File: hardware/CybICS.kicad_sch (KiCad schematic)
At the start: 64 parts, among them J1 Raspberry_Pi_2_3, J2 Conn_01x03_Pin, J3 Conn_01x05_Pin, SW1 SW_Push, SW2 SW_Push, U1 STM32G070RBTx

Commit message: Updated hardware
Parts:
- added R28: 10kR, Resistor_SMD:R_0805_2012Metric_Pad1.20x1.40mm_HandSolder, symbol Device:R
- J1: footprint Connector_PinHeader_2.54mm:PinHeader_2x20_P2.54mm_Vertical -> Module:Raspberry_Pi_Zero_Socketed_THT_FaceDown_MountingHoles
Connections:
- net GND: now also R28.2
- net PC10: now also R28.1
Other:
- moved on the sheet: R27, SW2
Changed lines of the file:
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@@
   (junction (at 64.77 24.13) (diameter 0) (color 0 0 0 0)
   )
+  (junction (at 156.21 181.61) (diameter 0) (color 0 0 0 0)
+  )
   (junction (at 161.29 100.33) (diameter 0) (color 0 0 0 0)
   )
@@
     (stroke (width 0) (type default))
   )
-  (wire (pts (xy 134.62 181.61) (xy 134.62 179.07))
+  (wire (pts (xy 165.1 171.45) (xy 165.1 170.18))
     (stroke (width 0) (type default))
   )
@@
     (stroke (width 0) (type default))
   )
-  (wire (pts (xy 123.19 191.77) (xy 134.62 191.77))
+  (wire (pts (xy 153.67 181.61) (xy 156.21 181.61))
     (stroke (width 0) (type default))
   )
@@
     (stroke (width 0) (type default))
   )
-  (polyline (pts (xy 113.03 140.97) (xy 113.03 196.85))
+  (polyline (pts (xy 113.03 140.97) (xy 113.03 170.18))
     (stroke (width 0) (type default))
   )
@@
     (stroke (width 0) (type default))
   )
+  (wire (pts (xy 156.21 181.61) (xy 165.1 181.61))
+    (stroke (width 0) (type default))
+  )
   (wire (pts (xy 271.78 149.86) (xy 281.94 149.86))
     (stroke (width 0) (type default))
@@
     (stroke (width 0) (type default))
   )
+  (polyline (pts (xy 146.05 160.02) (xy 180.34 160.02))
+    (stroke (width 0) (type default))
+  )
   (wire (pts (xy 271.78 152.4) (xy 281.94 152.4))
     (stroke (width 0) (type default))
@@
     (stroke (width 0) (type default))
   )
-  (wire (pts (xy 132.08 181.61) (xy 134.62 181.61))
+  (wire (pts (xy 162.56 171.45) (xy 165.1 171.45))
     (stroke (width 0) (type default))
   )
@@
     (stroke (width 0) (type default))
   )
-  (wire (pts (xy 124.46 181.61) (xy 123.19 181.61))
+  (wire (pts (xy 154.94 171.45) (xy 153.67 171.45))
     (stroke (width 0) (type default))
   )
@@
     (effects (font (size 1.27 1.27)) (justify left bottom))
   )
-  (text "Button" (at 114.3 172.72 0)
+  (text "Button" (at 147.32 163.83 0)
     (effects (font (size 1.27 1.27)) (justify left bottom))
   )
@@
     (effects (font (size 1.27 1.27)) (justify left bottom))
   )
-  (label "PC10" (at 129.54 191.77 0) (fields_autoplaced)
+  (label "PC10" (at 160.02 181.61 0) (fields_autoplaced)
     (effects (font (size 1.27 1.27)) (justify left bottom))
   )
@@
     )
   )
+  (symbol (lib_id "Device:R") (at 156.21 185.42 0) (unit 1)
+    (in_bom yes) (on_board yes) (dnp no)
+    (property "Reference" "R28" (at 158.75 184.15 0)
+      (effects (font (size 1.27 1.27)) (justify left))
+    )
+    (property "Value" "10kR" (at 158.75 186.69 0)
+      (effects (font (size 1.27 1.27)) (justify left))
+    )
+    (property "Footprint" "Resistor_SMD:R_0805_2012Metric_Pad1.20x1.40mm_HandSolder" (at 154.432 185.42 90)
+      (effects (font (size 1.27 1.27)) hide)
+    )
+    (property "Datasheet" "~" (at 156.21 185.42 0)
+      (effects (font (size 1.27 1.27)) hide)
+    )
+    (property "JLCPCB Part #" "C17513" (at 156.21 185.42 90)
+      (effects (font (size 1.27 1.27)) hide)
+    )
+    (pin "2")
+    (pin "1")
+    (instances
+      (project "CybICS"
+        (path "/8fcde287-628f-41a4-bd3a-47641b4dabbc"
+          (reference "R28") (unit 1)
+        )
+      )
+    )
+  )
   (symbol (lib_id "Device:R") (at 88.9 153.67 90) (unit 1)
     (in_bom yes) (on_board yes) (dnp no) (fields_autoplaced)
@@
     )
   )
-  (symbol (lib_id "Switch:SW_Push") (at 123.19 186.69 90) (unit 1)
+  (symbol (lib_id "Switch:SW_Push") (at 153.67 176.53 90) (unit 1)
     (in_bom yes) (on_board yes) (dnp no) (fields_autoplaced)
-    (property "Reference" "SW2" (at 124.46 185.42 90)
+    (property "Reference" "SW2" (at 154.94 175.26 90)
       (effects (font (size 1.27 1.27)) (justify right))
     )
-    (property "Value" "SW_Push" (at 124.46 187.96 90)
+    (property "Value" "SW_Push" (at 154.94 177.8 90)
       (effects (font (size 1.27 1.27)) (justify right))
     )
-    (property "Footprint" "Button_Switch_THT:SW_PUSH_6mm_H5mm" (at 118.11 186.69 0)
+    (property "Footprint" "Button_Switch_THT:SW_PUSH_6mm_H5mm" (at 148.59 176.53 0)
       (effects (font (size 1.27 1.27)) hide)
     )
-    (property "Datasheet" "~" (at 118.11 186.69 0)
+    (property "Datasheet" "~" (at 148.59 176.53 0)
       (effects (font (size 1.27 1.27)) hide)
     )
-    (property "JLCPCB Part #" "C428628" (at 123.19 186.69 90)
+    (property "JLCPCB Part #" "C428628" (at 153.67 176.53 90)
       (effects (font (size 1.27 1.27)) hide)
     )
@@
     )
   )
+  (symbol (lib_id "power:GND") (at 156.21 189.23 0) (unit 1)
+    (in_bom yes) (on_board yes) (dnp no) (fields_autoplaced)
+    (property "Reference" "#PWR041" (at 156.21 195.58 0)
+      (effects (font (size 1.27 1.27)) hide)
+    )
+    (property "Value" "GND" (at 156.21 194.31 0)
+      (effects (font (size 1.27 1.27)))
+    )
+    (property "Footprint" "" (at 156.21 189.23 0)
+      (effects (font (size 1.27 1.27)) hide)
+    )
+    (property "Datasheet" "" (at 156.21 189.23 0)
+      (effects (font (size 1.27 1.27)) hide)
+    )
+    (pin "1")
+    (instances
+      (project "CybICS"
+        (path "/8fcde287-628f-41a4-bd3a-47641b4dabbc"
+          (reference "#PWR041") (unit 1)
+        )
+      )
+    )
+  )
   (symbol (lib_id "power:+3V3") (at 73.66 162.56 0) (unit 1)
     (in_bom yes) (on_board yes) (dnp no) (fields_autoplaced)
@@
       (effects (font (size 1.27 1.27)) (justify left))
     )
-    (property "Footprint" "Connector_PinHeader_2.54mm:PinHeader_2x20_P2.54mm_Vertical" (at 166.37 67.31 0)
+    (property "Footprint" "Module:Raspberry_Pi_Zero_Socketed_THT_FaceDown_MountingHoles" (at 166.37 67.31 0)
       (effects (font (size 1.27 1.27)) hide)
     )
@@
     )
   )
-  (symbol (lib_id "power:+3V3") (at 134.62 179.07 0) (unit 1)
+  (symbol (lib_id "power:+3V3") (at 165.1 170.18 0) (unit 1)
     (in_bom yes) (on_board yes) (dnp no) (fields_autoplaced)
-    (property "Reference" "#PWR039" (at 134.62 182.88 0)
+    (property "Reference" "#PWR039" (at 165.1 173.99 0)
       (effects (font (size 1.27 1.27)) hide)
     )
-    (property "Value" "+3V3" (at 134.62 173.99 0)
+    (property "Value" "+3V3" (at 165.1 165.1 0)
       (effects (font (size 1.27 1.27)))
     )
-    (property "Footprint" "" (at 134.62 179.07 0)
+    (property "Footprint" "" (at 165.1 170.18 0)
       (effects (font (size 1.27 1.27)) hide)
     )
-    (property "Datasheet" "" (at 134.62 179.07 0)
+    (property "Datasheet" "" (at 165.1 170.18 0)
       (effects (font (size 1.27 1.27)) hide)
     )
@@
     )
   )
-  (symbol (lib_id "Device:R") (at 128.27 181.61 270) (unit 1)
+  (symbol (lib_id "Device:R") (at 158.75 171.45 270) (unit 1)
     (in_bom yes) (on_board yes) (dnp no) (fields_autoplaced)
-    (property "Reference" "R27" (at 128.27 175.26 90)
+    (property "Reference" "R27" (at 158.75 165.1 90)
       (effects (font (size 1.27 1.27)))
     )
-    (property "Value" "1kR" (at 128.27 177.8 90)
+    (property "Value" "1kR" (at 158.75 167.64 90)
       (effects (font (size 1.27 1.27)))
     )
-    (property "Footprint" "Resistor_SMD:R_0805_2012Metric_Pad1.20x1.40mm_HandSolder" (at 128.27 179.832 90)
+    (property "Footprint" "Resistor_SMD:R_0805_2012Metric_Pad1.20x1.40mm_HandSolder" (at 158.75 169.672 90)
       (effects (font (size 1.27 1.27)) hide)
     )
-    (property "Datasheet" "~" (at 128.27 181.61 0)
+    (property "Datasheet" "~" (at 158.75 171.45 0)
       (effects (font (size 1.27 1.27)) hide)
     )
-    (property "JLCPCB Part #" "C17513" (at 128.27 181.61 90)
+    (property "JLCPCB Part #" "C17513" (at 158.75 171.45 90)
       (effects (font (size 1.27 1.27)) hide)
     )

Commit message: Updated hardware
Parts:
- added R29, R30, R31, R32, R33, R34, R35, R36: 10kR, Resistor_SMD:R_0805_2012Metric_Pad1.20x1.40mm_HandSolder, symbol Device:R
- added R37: 1kR, Resistor_SMD:R_0805_2012Metric_Pad1.20x1.40mm_HandSolder, symbol Device:R
- added SW3: SW_Push, Button_Switch_THT:SW_PUSH_6mm_H5mm, symbol Switch:SW_Push
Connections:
- net +3V3: now also R37.1
- net GND: now also R29.2, R30.2, R31.2, R32.2, R33.2, R34.2, R35.2, R36.2
- net PA0: now also R29.1
- net PA1: now also R30.1
- net PA2: now also R31.1
- net PA3: now also R32.1
- net PA4: now also R33.1
- net PA5: now also R34.1
- net PA6: now also R35.1
- net PA8: now reaches U1.36 (PA8)
- net PA8: now also R36.1, SW3.1
- new net: R37.2, SW3.2
- no-connect marks 40 -> 39
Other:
- note added: "Pulldowns"

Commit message: Add testing for i2c communication
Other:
- note added: "Button Display"
- moved on the sheet: DS1, R36, R37, RV1, SW3

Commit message: Updated documentation and preparing signals for OpenPLC
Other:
- note added: "BO_sen"
- note added: "C_sig"
- note added: "SV_sig"
- note added: "S_sen"
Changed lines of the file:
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@@
+    (effects (font (size 1.27 1.27)) (justify left bottom))
+  )
+  (text "C_sig" (at 194.31 72.39 0)
+    (effects (font (size 1.27 1.27)) (justify left bottom))
+  )
+  (text "SV_sig" (at 194.31 69.85 0)
+    (effects (font (size 1.27 1.27)) (justify left bottom))
+  )
+  (text "S_sen" (at 194.31 46.99 0)
+    (effects (font (size 1.27 1.27)) (justify left bottom))
+  )
+  (text "BO_sen" (at 194.31 85.09 0)
     (effects (font (size 1.27 1.27)) (justify left bottom))
   )

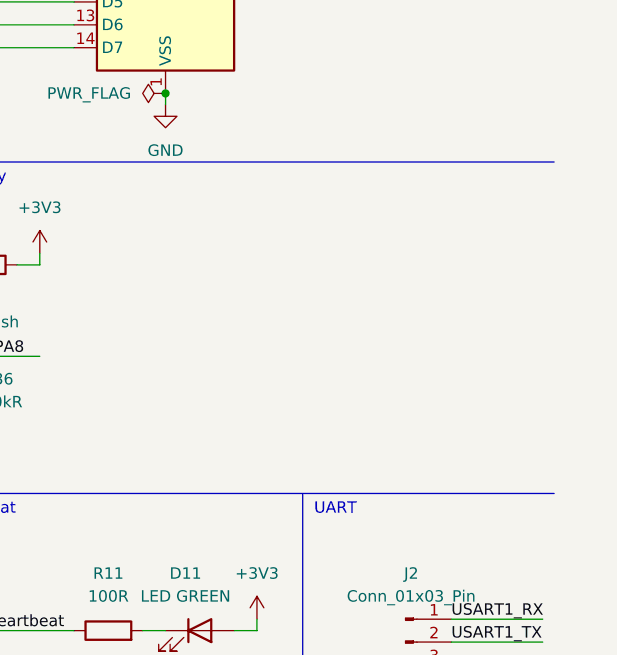
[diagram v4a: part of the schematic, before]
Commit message: This commit will: - fix #2 - Added usb-c (only for power supply) - Added first attack example
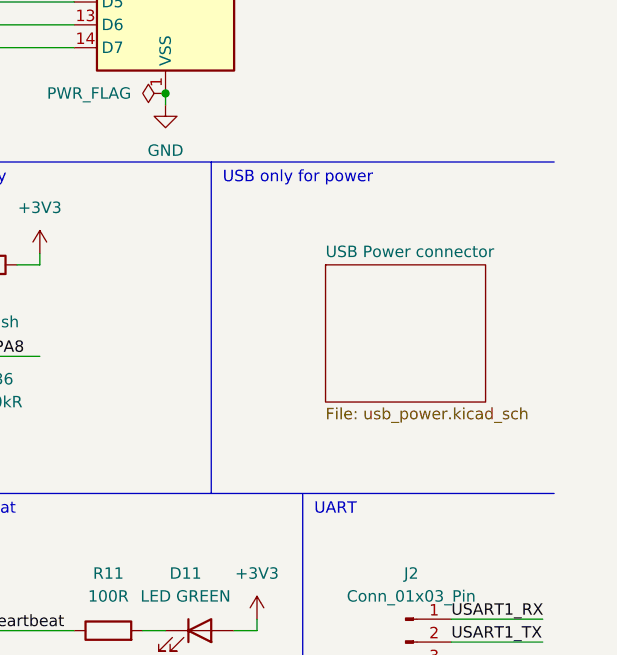
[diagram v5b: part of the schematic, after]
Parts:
- R28, R29, R30, R31, R32, R33, R34, R35, R36: JLCPCB Part # C17513 -> C17414
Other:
- added sheet USB Power connector (usb_power.kicad_sch)
- note added: "USB only for power"
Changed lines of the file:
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@@
     (stroke (width 0) (type default))
   )
+  (polyline (pts (xy 246.38 69.85) (xy 246.38 106.68))
+    (stroke (width 0) (type default))
+  )
   (polyline (pts (xy 256.54 106.68) (xy 256.54 165.1))
     (stroke (width 0) (type default))
@@
     (effects (font (size 1.27 1.27)) (justify left bottom))
   )
+  (text "USB only for power" (at 247.65 72.39 0)
+    (effects (font (size 1.27 1.27)) (justify left bottom))
+  )
   (text "Blowout" (at 13.97 143.51 0)
     (effects (font (size 1.27 1.27)) (justify left bottom))
@@
       (effects (font (size 1.27 1.27)) hide)
     )
-    (property "JLCPCB Part #" "C17513" (at 156.21 185.42 90)
+    (property "JLCPCB Part #" "C17414" (at 156.21 185.42 90)
       (effects (font (size 1.27 1.27)) hide)
     )
@@
       (effects (font (size 1.27 1.27)) hide)
     )
-    (property "JLCPCB Part #" "C17513" (at 102.87 190.5 90)
+    (property "JLCPCB Part #" "C17414" (at 102.87 190.5 90)
       (effects (font (size 1.27 1.27)) hide)
     )
@@
       (effects (font (size 1.27 1.27)) hide)
     )
-    (property "JLCPCB Part #" "C17513" (at 80.01 175.26 90)
+    (property "JLCPCB Part #" "C17414" (at 80.01 175.26 90)
       (effects (font (size 1.27 1.27)) hide)
     )
@@
       (effects (font (size 1.27 1.27)) hide)
     )
-    (property "JLCPCB Part #" "C17513" (at 102.87 182.88 90)
+    (property "JLCPCB Part #" "C17414" (at 102.87 182.88 90)
       (effects (font (size 1.27 1.27)) hide)
     )
@@
       (effects (font (size 1.27 1.27)) hide)
     )
-    (property "JLCPCB Part #" "C17513" (at 218.44 95.25 90)
+    (property "JLCPCB Part #" "C17414" (at 218.44 95.25 90)
       (effects (font (size 1.27 1.27)) hide)
     )
@@
       (effects (font (size 1.27 1.27)) hide)
     )
-    (property "JLCPCB Part #" "C17513" (at 80.01 182.88 90)
+    (property "JLCPCB Part #" "C17414" (at 80.01 182.88 90)
       (effects (font (size 1.27 1.27)) hide)
     )
@@
       (effects (font (size 1.27 1.27)) hide)
     )
-    (property "JLCPCB Part #" "C17513" (at 102.87 175.26 90)
+    (property "JLCPCB Part #" "C17414" (at 102.87 175.26 90)
       (effects (font (size 1.27 1.27)) hide)
     )
@@
       (effects (font (size 1.27 1.27)) hide)
     )
-    (property "JLCPCB Part #" "C17513" (at 125.73 175.26 90)
+    (property "JLCPCB Part #" "C17414" (at 125.73 175.26 90)
       (effects (font (size 1.27 1.27)) hide)
     )
@@
       (effects (font (size 1.27 1.27)) hide)
     )
-    (property "JLCPCB Part #" "C17513" (at 80.01 190.5 90)
+    (property "JLCPCB Part #" "C17414" (at 80.01 190.5 90)
       (effects (font (size 1.27 1.27)) hide)
     )
@@
       )
     )
+  )
+  (sheet (at 259.08 81.28) (size 17.78 15.24) (fields_autoplaced)
+    (stroke (width 0.1524) (type solid))
+    (fill (color 0 0 0 0.0000))
+    (property "Sheetname" "USB Power connector" (at 259.08 80.5684 0)
+      (effects (font (size 1.27 1.27)) (justify left bottom))
+    )
+    (property "Sheetfile" "usb_power.kicad_sch" (at 259.08 97.1046 0)
+      (effects (font (size 1.27 1.27)) (justify left top))
+    )
+    (instances
+      (project "CybICS"
+        (path "/8fcde287-628f-41a4-bd3a-47641b4dabbc" (page "2"))
+      )
+    )

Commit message: Hardware change for version 0.2
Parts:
- R1, R10, R2, R21, R23, R25, R4, R5, R6, R8: value 100R -> 330R; JLCPCB Part # C17408 -> C52548
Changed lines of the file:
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@@
       (effects (font (size 1.27 1.27)))
     )
-    (property "Value" "100R" (at 125.73 116.84 90)
+    (property "Value" "330R" (at 125.73 116.84 90)
       (effects (font (size 1.27 1.27)))
     )
@@
       (effects (font (size 1.27 1.27)) hide)
     )
-    (property "JLCPCB Part #" "C17408" (at 125.73 120.65 90)
+    (property "JLCPCB Part #" "C52548" (at 125.73 120.65 90)
       (effects (font (size 1.27 1.27)) hide)
     )
@@
       (effects (font (size 1.27 1.27)))
     )
-    (property "Value" "100R" (at 88.9 149.86 90)
+    (property "Value" "330R" (at 88.9 149.86 90)
       (effects (font (size 1.27 1.27)))
     )
@@
       (effects (font (size 1.27 1.27)) hide)
     )
-    (property "JLCPCB Part #" "C17408" (at 88.9 153.67 90)
+    (property "JLCPCB Part #" "C52548" (at 88.9 153.67 90)
       (effects (font (size 1.27 1.27)) hide)
     )
@@
       (effects (font (size 1.27 1.27)))
     )
-    (property "Value" "100R" (at 57.15 149.86 90)
+    (property "Value" "330R" (at 57.15 149.86 90)
       (effects (font (size 1.27 1.27)))
     )
@@
       (effects (font (size 1.27 1.27)) hide)
     )
-    (property "JLCPCB Part #" "C17408" (at 57.15 153.67 90)
+    (property "JLCPCB Part #" "C52548" (at 57.15 153.67 90)
       (effects (font (size 1.27 1.27)) hide)
     )
@@
       (effects (font (size 1.27 1.27)))
     )
-    (property "Value" "100R" (at 125.73 128.27 90)
+    (property "Value" "330R" (at 125.73 128.27 90)
       (effects (font (size 1.27 1.27)))
     )
@@
       (effects (font (size 1.27 1.27)) hide)
     )
-    (property "JLCPCB Part #" "C17408" (at 125.73 132.08 90)
+    (property "JLCPCB Part #" "C52548" (at 125.73 132.08 90)
       (effects (font (size 1.27 1.27)) hide)
     )
@@
       (effects (font (size 1.27 1.27)))
     )
-    (property "Value" "100R" (at 125.73 162.56 90)
+    (property "Value" "330R" (at 125.73 162.56 90)
       (effects (font (size 1.27 1.27)))
     )
@@
       (effects (font (size 1.27 1.27)) hide)
     )
-    (property "JLCPCB Part #" "C17408" (at 125.73 166.37 90)
+    (property "JLCPCB Part #" "C52548" (at 125.73 166.37 90)
       (effects (font (size 1.27 1.27)) hide)
     )
@@
       (effects (font (size 1.27 1.27)))
     )
-    (property "Value" "100R" (at 24.13 149.86 90)
+    (property "Value" "330R" (at 24.13 149.86 90)
       (effects (font (size 1.27 1.27)))
     )
@@
       (effects (font (size 1.27 1.27)) hide)
     )
-    (property "JLCPCB Part #" "C17408" (at 24.13 153.67 90)
+    (property "JLCPCB Part #" "C52548" (at 24.13 153.67 90)
       (effects (font (size 1.27 1.27)) hide)
     )
@@
       (effects (font (size 1.27 1.27)))
     )
-    (property "Value" "100R" (at 191.77 129.54 90)
+    (property "Value" "330R" (at 191.77 129.54 90)
       (effects (font (size 1.27 1.27)))
     )
@@
       (effects (font (size 1.27 1.27)) hide)
     )
-    (property "JLCPCB Part #" "C17408" (at 191.77 133.35 90)
+    (property "JLCPCB Part #" "C52548" (at 191.77 133.35 90)
       (effects (font (size 1.27 1.27)) hide)
     )
@@
       (effects (font (size 1.27 1.27)))
     )
-    (property "Value" "100R" (at 160.02 138.43 90)
+    (property "Value" "330R" (at 160.02 138.43 90)
       (effects (font (size 1.27 1.27)))
     )
@@
       (effects (font (size 1.27 1.27)) hide)
     )
-    (property "JLCPCB Part #" "C17408" (at 160.02 142.24 90)
+    (property "JLCPCB Part #" "C52548" (at 160.02 142.24 90)
       (effects (font (size 1.27 1.27)) hide)
     )
@@
       (effects (font (size 1.27 1.27)))
     )
-    (property "Value" "100R" (at 125.73 151.13 90)
+    (property "Value" "330R" (at 125.73 151.13 90)
       (effects (font (size 1.27 1.27)))
     )
@@
       (effects (font (size 1.27 1.27)) hide)
     )
-    (property "JLCPCB Part #" "C17408" (at 125.73 154.94 90)
+    (property "JLCPCB Part #" "C52548" (at 125.73 154.94 90)
       (effects (font (size 1.27 1.27)) hide)
     )
@@
       (effects (font (size 1.27 1.27)))
     )
-    (property "Value" "100R" (at 160.02 118.11 90)
+    (property "Value" "330R" (at 160.02 118.11 90)
       (effects (font (size 1.27 1.27)))
     )
@@
       (effects (font (size 1.27 1.27)) hide)
     )
-    (property "JLCPCB Part #" "C17408" (at 160.02 121.92 90)
+    (property "JLCPCB Part #" "C52548" (at 160.02 121.92 90)
       (effects (font (size 1.27 1.27)) hide)
     )

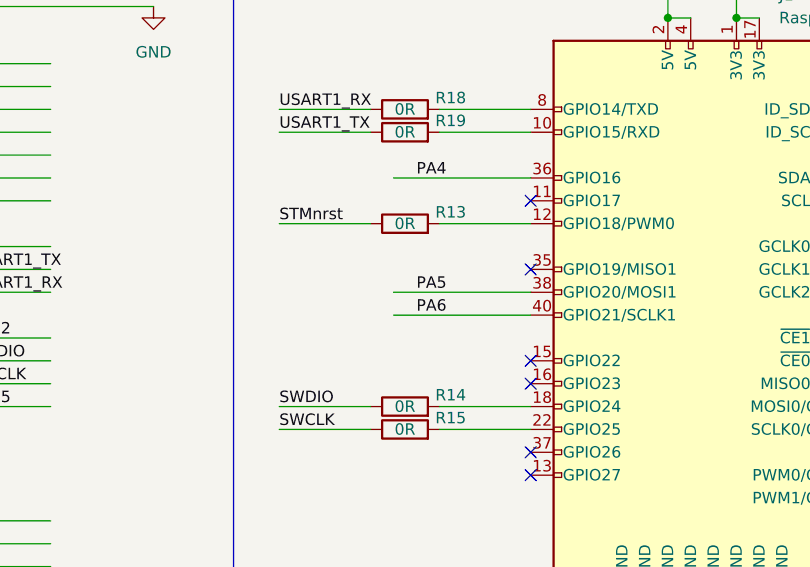
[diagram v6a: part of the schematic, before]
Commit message: Updated GST behaviour on physical process
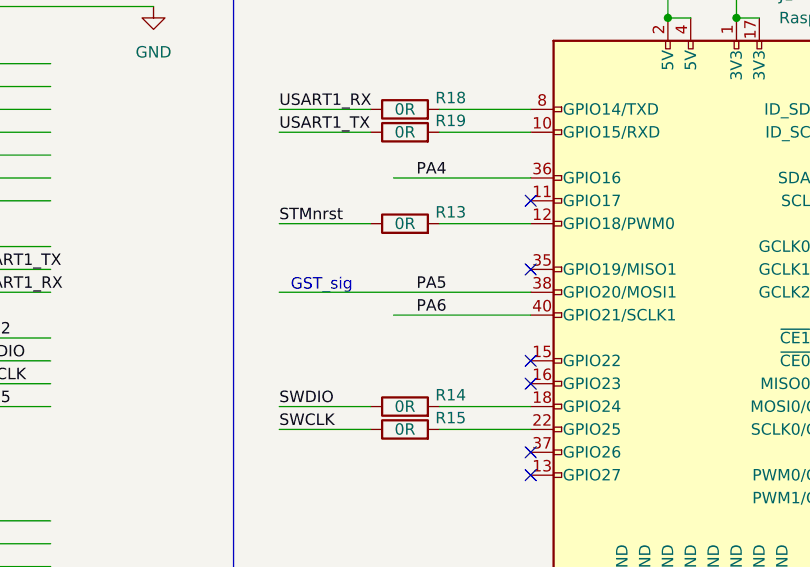
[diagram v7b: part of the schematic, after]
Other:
- note added: "GST_sig"
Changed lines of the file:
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@@
+    (stroke (width 0) (type default))
+  )
+  (wire (pts (xy 118.11 64.77) (xy 146.05 64.77))
     (stroke (width 0) (type default))
   )
@@
     (stroke (width 0) (type default))
   )
-  (wire (pts (xy 130.81 64.77) (xy 146.05 64.77))
-    (stroke (width 0) (type default))
-  )
   (wire (pts (xy 93.98 182.88) (xy 99.06 182.88))
     (stroke (width 0) (type default))
@@
     (effects (font (size 1.27 1.27)) (justify left bottom))
   )
+  (text "GST_sig" (at 119.38 64.77 0)
+    (effects (font (size 1.27 1.27)) (justify left bottom))
+  )
